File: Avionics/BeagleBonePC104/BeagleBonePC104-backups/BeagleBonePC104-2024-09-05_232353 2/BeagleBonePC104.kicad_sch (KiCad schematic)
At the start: 14 parts, among them U4 TJA1051T-3, U5 TMP36xS

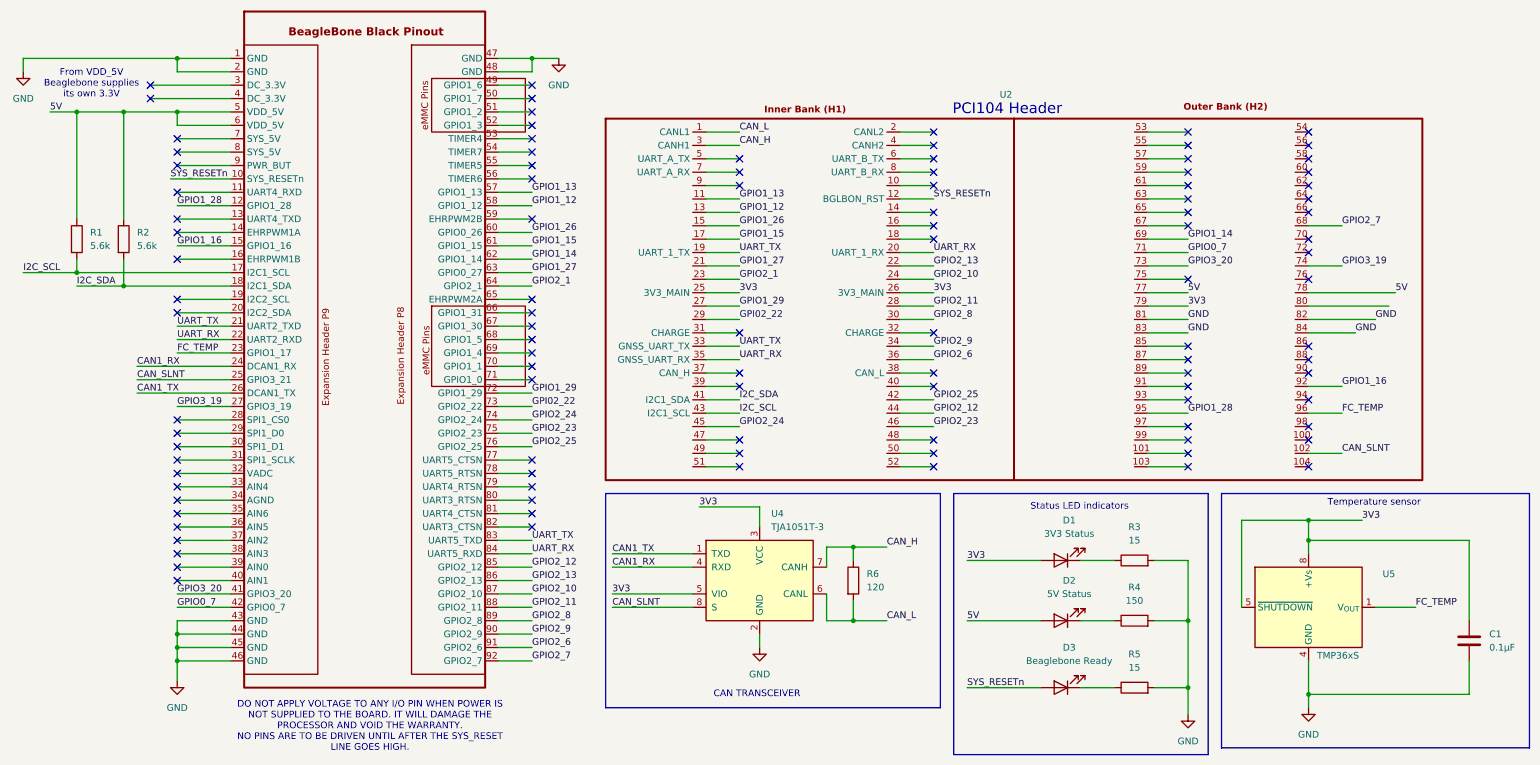
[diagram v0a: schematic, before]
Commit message: Ian Goldberg - Made changes to the third revision of the flight computer board, trying to figure out a way to power it throught ht header connector while still extracting data (through ethernet).
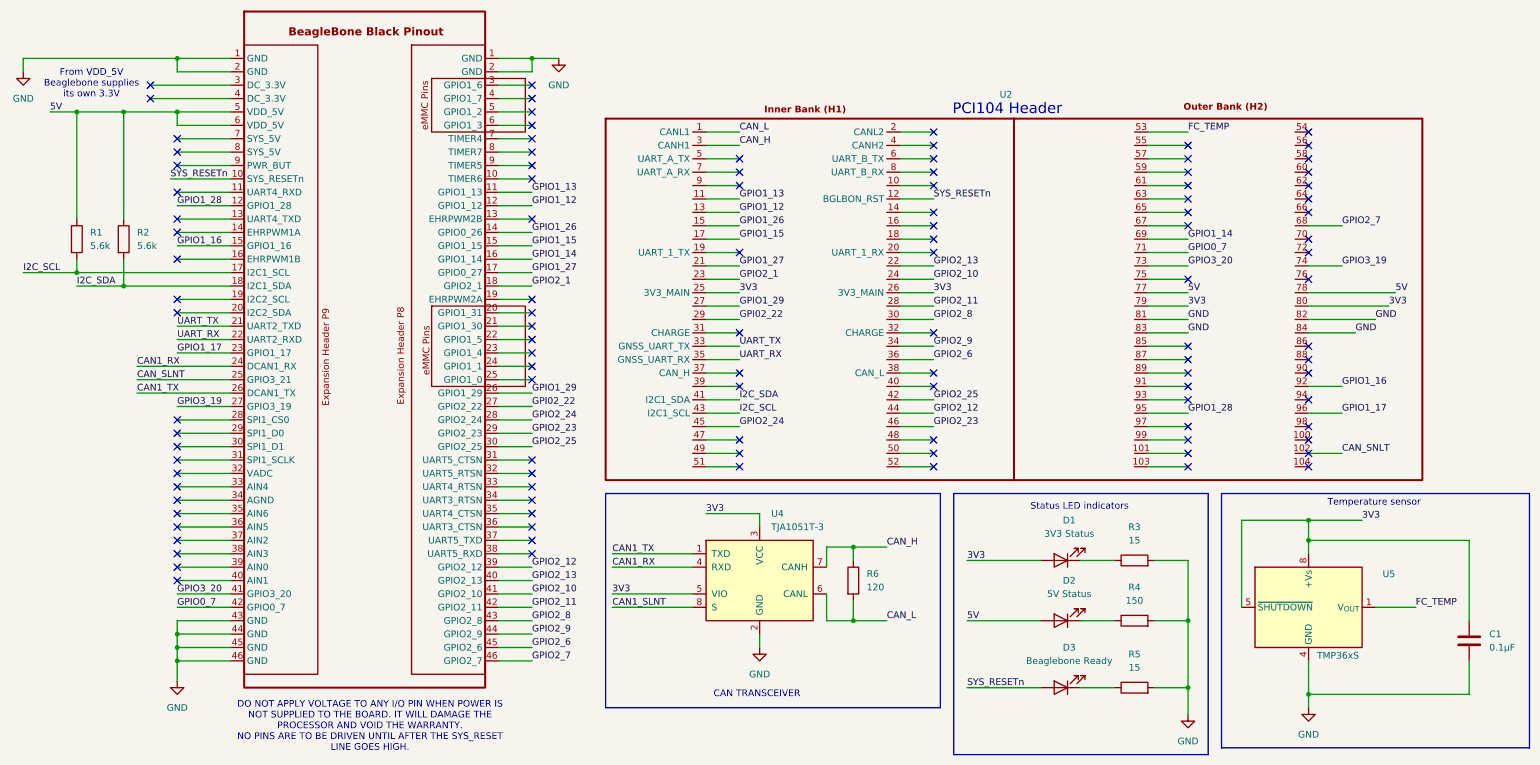
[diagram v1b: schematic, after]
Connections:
- net 3V3: now also U2.80
- net CAN_SLNT: no longer U2.102, U4.8 (S)
- net FC_TEMP: now also U2.53; no longer U1.23 (GPIO1_17), U2.96
- net GND: no longer U1.47 (GND), U1.48 (GND)
- net GPI02_22: now also U1.27 (GPIO3_19); no longer U1.73 (GPIO2_22)
- net GPIO1_12: now also U1.12 (GPIO1_28); no longer U1.58 (GPIO1_12)
- net GPIO1_13: now also U1.11 (UART4_RXD); no longer U1.57 (GPIO1_13)
- net GPIO1_14: now also U1.16 (GPIO1_14); no longer U1.62 (GPIO1_14)
- net GPIO1_15: now also U1.15 (GPIO1_16); no longer U1.61 (GPIO1_15)
- net GPIO1_26: now also U1.14 (GPIO0_26); no longer U1.60 (GPIO0_26)
- net GPIO1_27: now also U1.17 (I2C1_SCL); no longer U1.63 (GPIO0_27)
- net GPIO1_29: now also U1.26 (GPIO1_29); no longer U1.72 (GPIO1_29)
- net GPIO2_1: now also U1.18 (I2C1_SDA); no longer U1.64 (GPIO2_1)
- net GPIO2_10: now also U1.41 (GPIO3_20); no longer U1.87 (GPIO2_10)
- net GPIO2_11: now also U1.42 (GPIO2_11); no longer U1.88 (GPIO2_11)
- net GPIO2_12: now also U1.39 (GPIO2_12); no longer U1.85 (GPIO2_12)
- net GPIO2_13: now also U1.40 (GPIO2_13); no longer U1.86 (GPIO2_13)
- net GPIO2_23: now also U1.29 (SPI1_D0); no longer U1.75 (GPIO2_23)
- net GPIO2_24: now also U1.28 (SPI1_CS0); no longer U1.74 (GPIO2_24)
- net GPIO2_25: now also U1.30 (SPI1_D1); no longer U1.76 (GPIO2_25)
- net GPIO2_6: now also U1.45 (GPIO2_6); no longer U1.91 (GPIO2_6)
- net GPIO2_7: now also U1.46 (GPIO2_7); no longer U1.92 (GPIO2_7)
- net GPIO2_8: now also U1.43 (GPIO2_8); no longer U1.89 (GPIO2_8)
- net GPIO2_9: now also U1.44 (GPIO2_9); no longer U1.90 (GPIO2_9)
- net UART_RX: no longer U1.84 (UART5_RXD), U2.20 (UART_1_RX)
- net UART_TX: no longer U1.83 (UART5_TXD), U2.19 (UART_1_TX)
- new net CAN1_SLNT: U4.8 (S)
- new net CAN_SNLT: U2.102
- new net GPIO1_17: U1.23 (GPIO1_4), U2.96
- no-connect marks 104 -> 108
